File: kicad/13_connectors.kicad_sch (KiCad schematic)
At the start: 20 parts, among them J2 UART 3V3, J3 2x19 1.27mm socket (bottom), J5 LCD 1x14 2.54mm, U1301 SN74AVC4T774RSVR

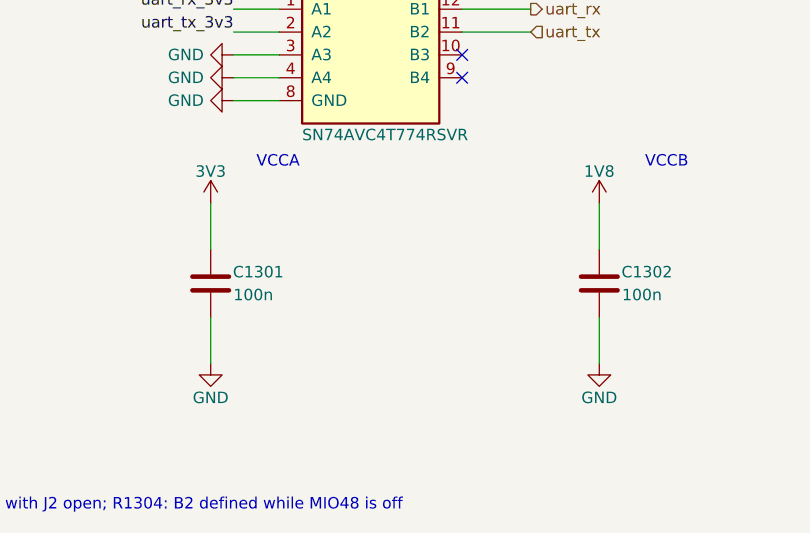
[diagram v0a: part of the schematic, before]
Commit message: Bottom-side heights checked (tools/check_heights.py), C67 22 uF 1206 (E12); RGMII TX series R at the SoC end
- tools/check_heights.py: the baseboard mapped through J11/J12, every card B.Cu part over a baseboard part within
  the 5.3 mm gap less 0.3 mm. C67 (100 uF 1210, 2.7 mm) over U17 (SOIC-16W) failed: now 22 uF 1206 CL31A226KAHNNNE
  (REUSE_LOG E12, user), 0.85 mm left; all pass. FP_SWAP in check_block_netlist.py, used by make_board/import_block.
  H1 push-pin barb over U17 fits (user).
- PHY area: TX series 22 R (R901-R906) moved from the PHY to B.Cu east of the block (sheet 9: TX at the SoC);
  R606 out of the eMMC ball field (placement/hand_fixes.sh).
- tools/sheets/_common.py: eeschema 10 sheets (no embedded_fonts) can be rebuilt again.
Checks: ERC 4 intended, block netlist and block copper 0 failures, DRC parity 0.

Co-Authored-By: Claude Opus 5.5 <noreply@anthropic.com>
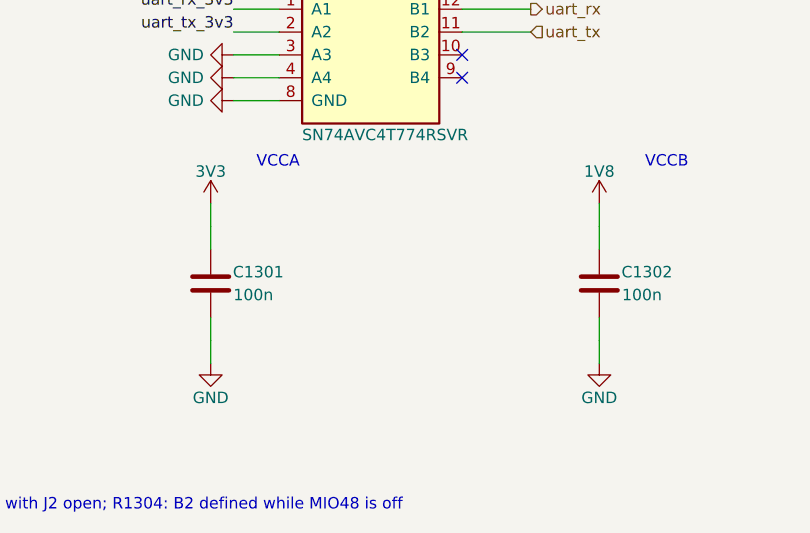
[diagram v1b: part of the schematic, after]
